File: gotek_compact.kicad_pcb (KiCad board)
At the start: 4 copper layers, 55 x 42 mm, 45 parts, among them CN1 POWER_IN, CN2 USB, CN3 Floppy 34, J1 Sound, J2 USB_Prog, J3 OLED+SER, J4 Encoder, Q1 MMBT3904, U1 STM32F105RBT6, U2 74LCX07, U3 AP2112K-3.3, X1 8MHz

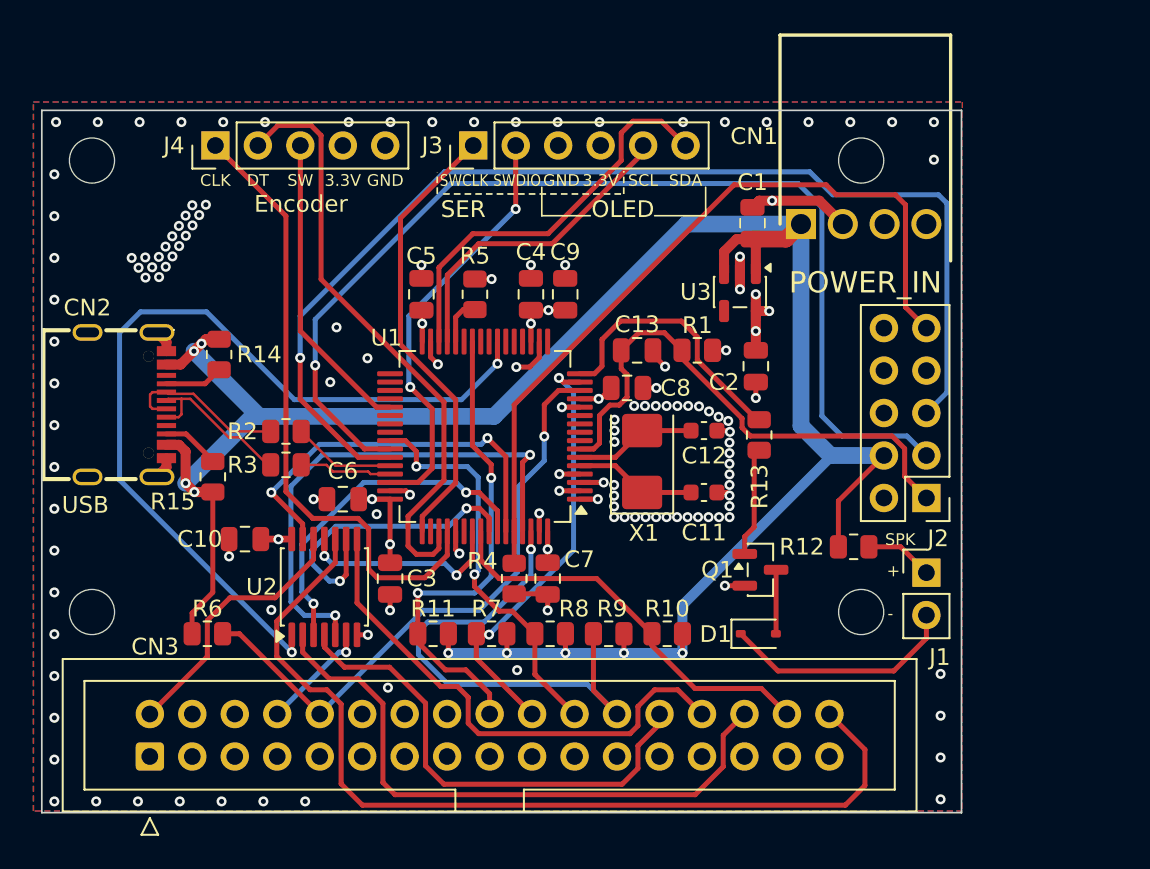
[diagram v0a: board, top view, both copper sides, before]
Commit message: PCB modified for the bracket options
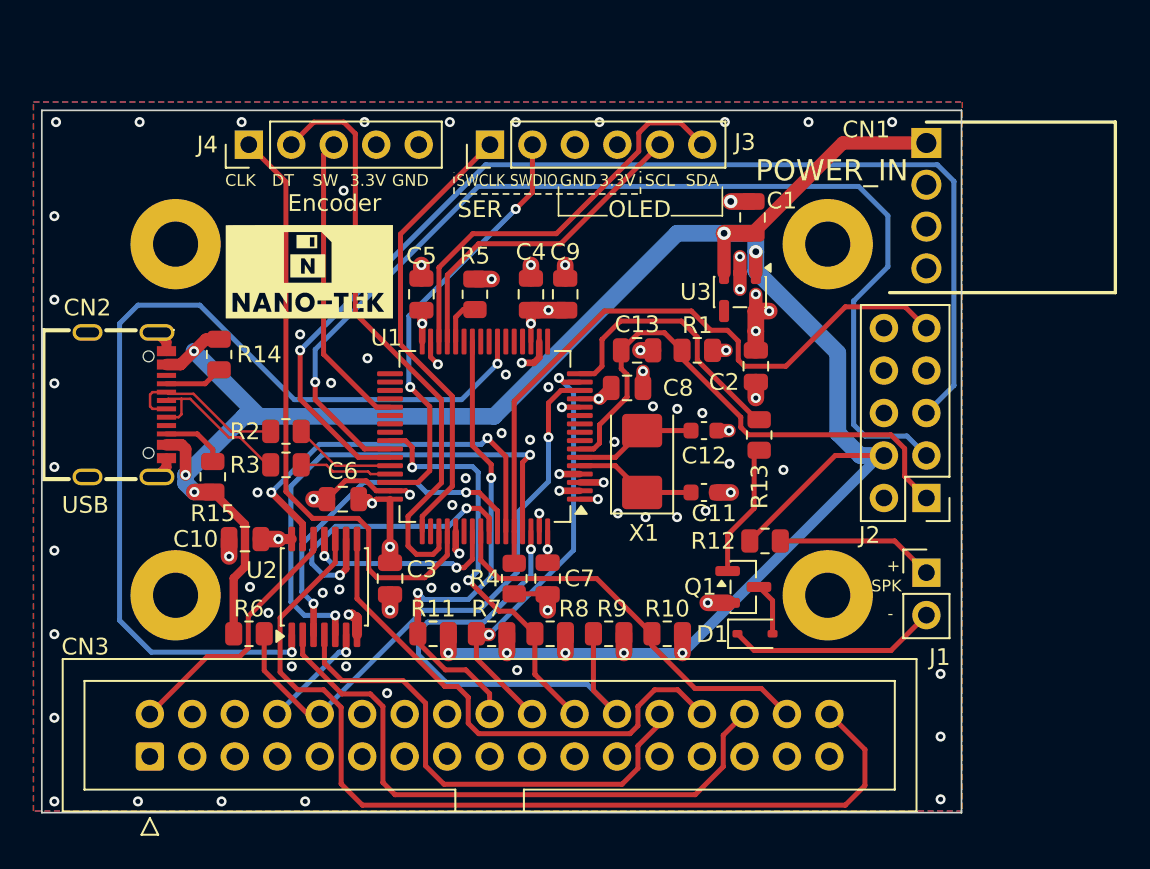
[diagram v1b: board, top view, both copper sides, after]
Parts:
- added LOGO1: LOGO, gotek_compact:NanoTek_Logo_Stacked_10mm, F.Cu at (56.0, 27.6)
- added LOGO2: NanoTek_Logo_Horizontal_Tagline, gotek_compact:NanoTek_Logo_Horizontal_Tagline, B.Cu at (67.5, 36.3)
- H1, H2, H3, H4: footprint MountingHole:MountingHole_2.7mm_M2.5 -> MountingHole:MountingHole_2.7mm_M2.5_Pad
- moved CN1 8.93 mm to (92.9, 19.9), turned to -90 degrees
- moved H1 7.07 mm to (48.0, 26.0)
- moved H4 5.39 mm to (87.0, 26.0)
- moved R12 5.31 mm to (83.2, 43.8)
- moved H2 5.10 mm to (48.0, 47.0)
- moved R6 2.49 mm to (52.4, 49.3)
- moved H3 2.24 mm to (87.0, 47.0)
- moved J4 2.00 mm to (52.4, 20.1)
- moved Q1 1.45 mm to (82.0, 46.5)
- moved J3 1.00 mm to (66.8, 20.1)
- moved C1 0.35 mm to (82.5, 24.4)
- moved D1 0.20 mm to (82.7, 49.3)
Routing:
- net +5V: track 137.9 -> 146.1 mm, vias 9 -> 10
- net BOOT0: track 46.7 -> 40.6 mm
- net _DKRD_3V: track 51.9 -> 57.5 mm
- net SPK+: track 4.08 -> 9.52 mm
- net RXD: track 64.5 -> 66.2 mm
- net SPK-: track 14.2 -> 12.6 mm
- net Net-(Q1-B): track 6.43 -> 7.88 mm
- net _SEL0: track 36.3 -> 35.0 mm
- net ENC_CLK: track 37.6 -> 36.9 mm
- net SCL: track 19.2 -> 19.9 mm
- net ENC_DT: track 36.2 -> 35.5 mm
- net _DKWD: track 23.9 -> 24.6 mm
- net Net-(D1-A): track 3.83 -> 3.14 mm
- net SDA: track 24.4 -> 24.9 mm
- net _TRK0: track 29.3 -> 29.8 mm
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
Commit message: Mounting holes adjusted
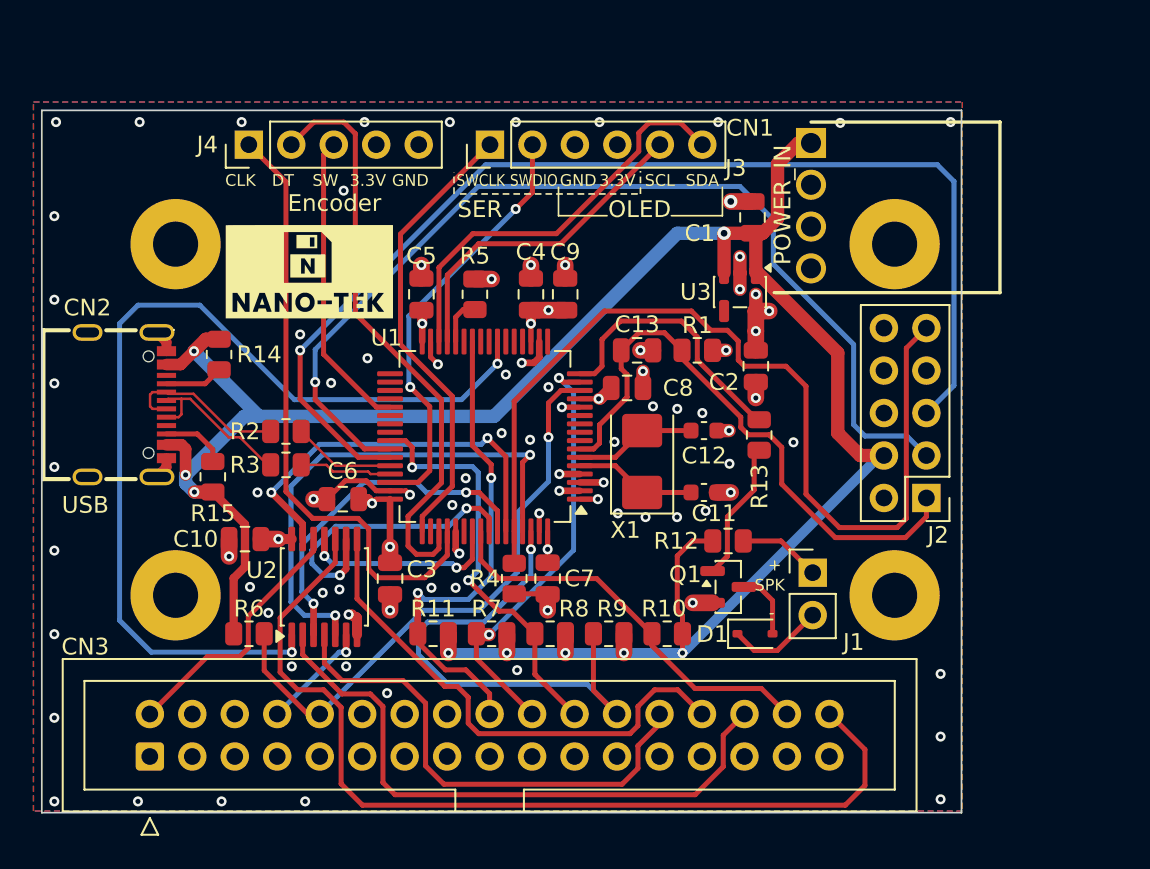
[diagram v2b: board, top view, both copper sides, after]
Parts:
- moved CN1 6.90 mm to (86.0, 19.9)
- moved J1 6.80 mm to (86.1, 45.6)
- moved H3 4.00 mm to (91.0, 47.0)
- moved H4 4.00 mm to (91.0, 26.0)
- moved R12 2.21 mm to (81.0, 43.8)
- moved Q1 0.90 mm to (81.0, 46.5)
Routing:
- net BOOT0: track 40.6 -> 57.3 mm
- net +5V: track 146.1 -> 135.3 mm, vias 10 -> 9
- net SPK-: track 12.6 -> 5.79 mm
- net RXD: track 66.2 -> 60.3 mm
- net SPK+: track 9.52 -> 4.93 mm
- net NRST: track 32.1 -> 35.0 mm
- net Net-(D1-A): track 3.14 -> 4.04 mm
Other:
- board text added: "Rev 1.0, July 2026 Schematics derived from OpenFlops design by SukkoPera Thanks to: Vinny, Mesarim, Screemo, Kavanoz, Wrangler, Ordyne"
